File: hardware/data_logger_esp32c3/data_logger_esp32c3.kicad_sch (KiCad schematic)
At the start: 74 parts, among them U1 ESP32-C3-MINI-1, U10 A03401A, U11 SX1509BIULTRT, U2 AZ1117IH-3.3TRG1, U4 LM321MF, U5 LM321MF, U6 LM321MF, U7 LM321MF, U8 LM321MF, U9 A03401A

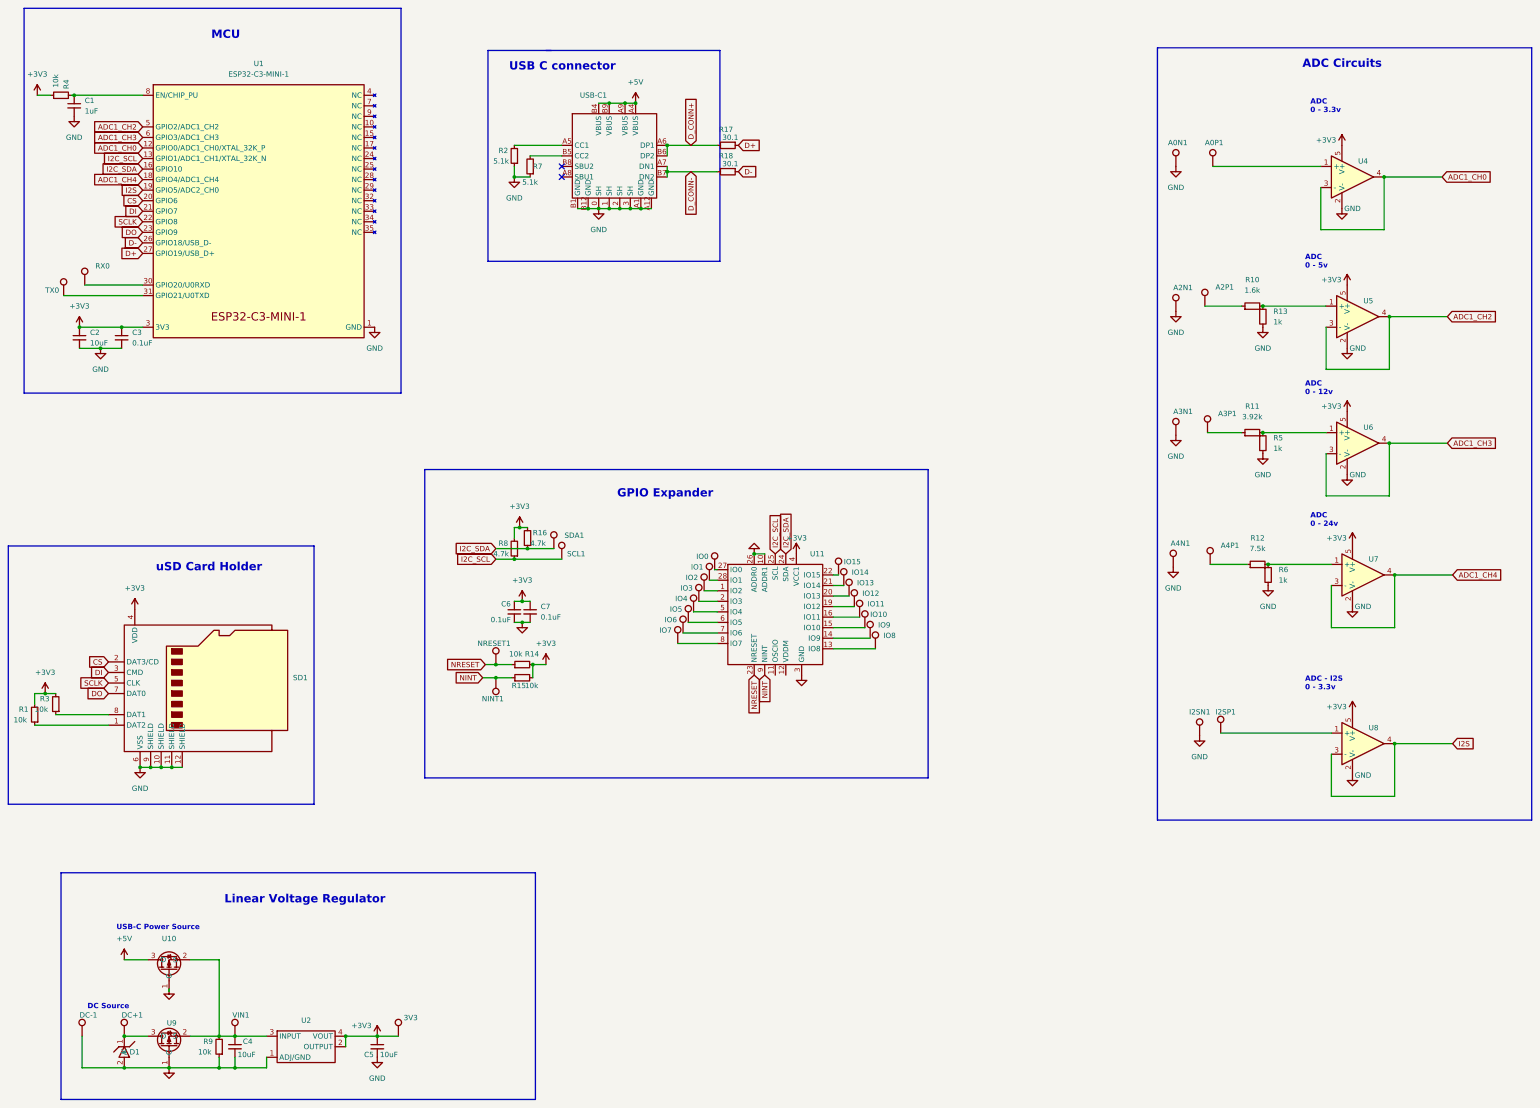
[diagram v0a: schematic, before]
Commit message: replaced adc with neopixel
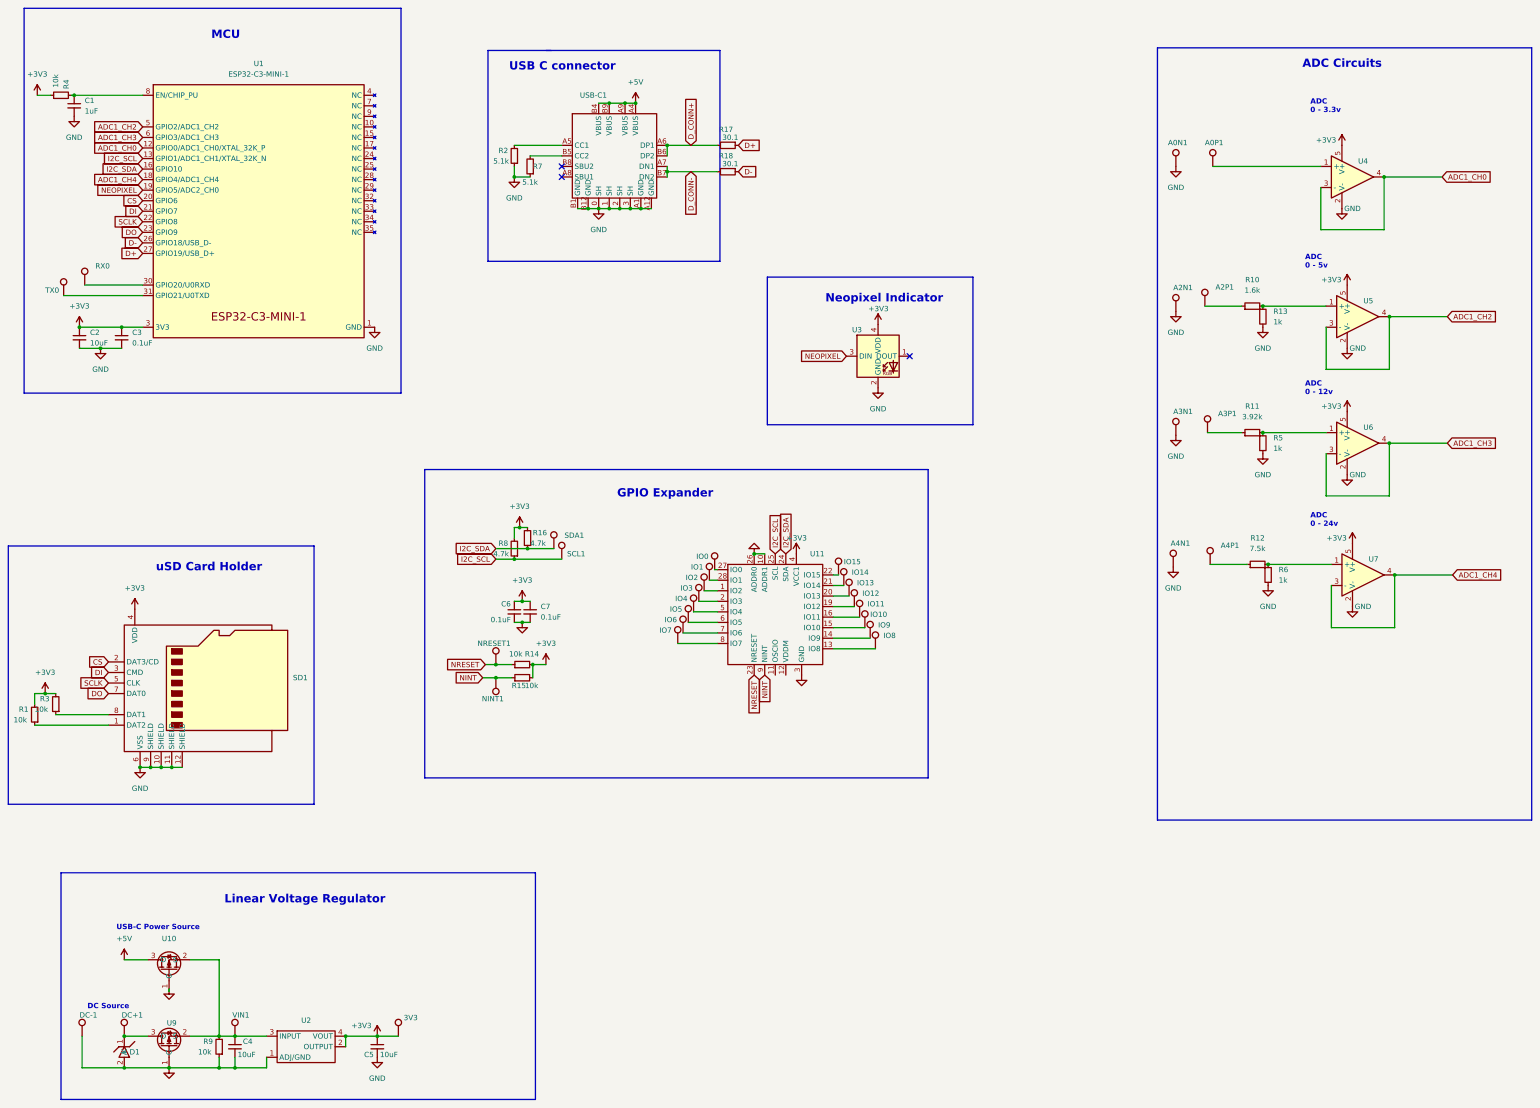
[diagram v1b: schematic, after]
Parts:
- removed I2SN1, I2SP1: TestPoint, TestPoint:TestPoint_THTPad_1.0x1.0mm_Drill0.5mm, symbol Connector:TestPoint
- removed U8: LM321MF, 1_project_footprints:LM321MF, symbol lib:LM321MF
- added U3: ~, 1_project_footprints:WS2812B-2020, symbol 1_project_specific:WS2812B-2020
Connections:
- net +3V3: now also U3.4 (VDD)
- net GND: now also U3.2 (GND)
- net I2S renamed NEOPIXEL
- net NEOPIXEL: now also U3.3 (DIN)
- no-connect marks 2 -> 3
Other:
- note added: "Neopixel Indicator"
- note removed: "ADC - I2S 0 - 3.3v"
